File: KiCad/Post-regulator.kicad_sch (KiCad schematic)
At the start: 111 parts, among them IC17 LTC2050HVCS8#PBF, IC18 TL072D, IC19 TL072D, IC20 SN74LVC1G3157DCKR, Q10 MMBT5401, Q11 MMBT5401, Q12 BCP56-16.115, Q13 MMBT5551, Q14 IRFP250NPBF, Q15 BCP56-16.115, Q16 BC857C, Q17 IRFI9Z34GPBF, Q18 PSMN0R9-25YLC, Q19 PSMN0R9-25YLC, Q9 MMBT5551

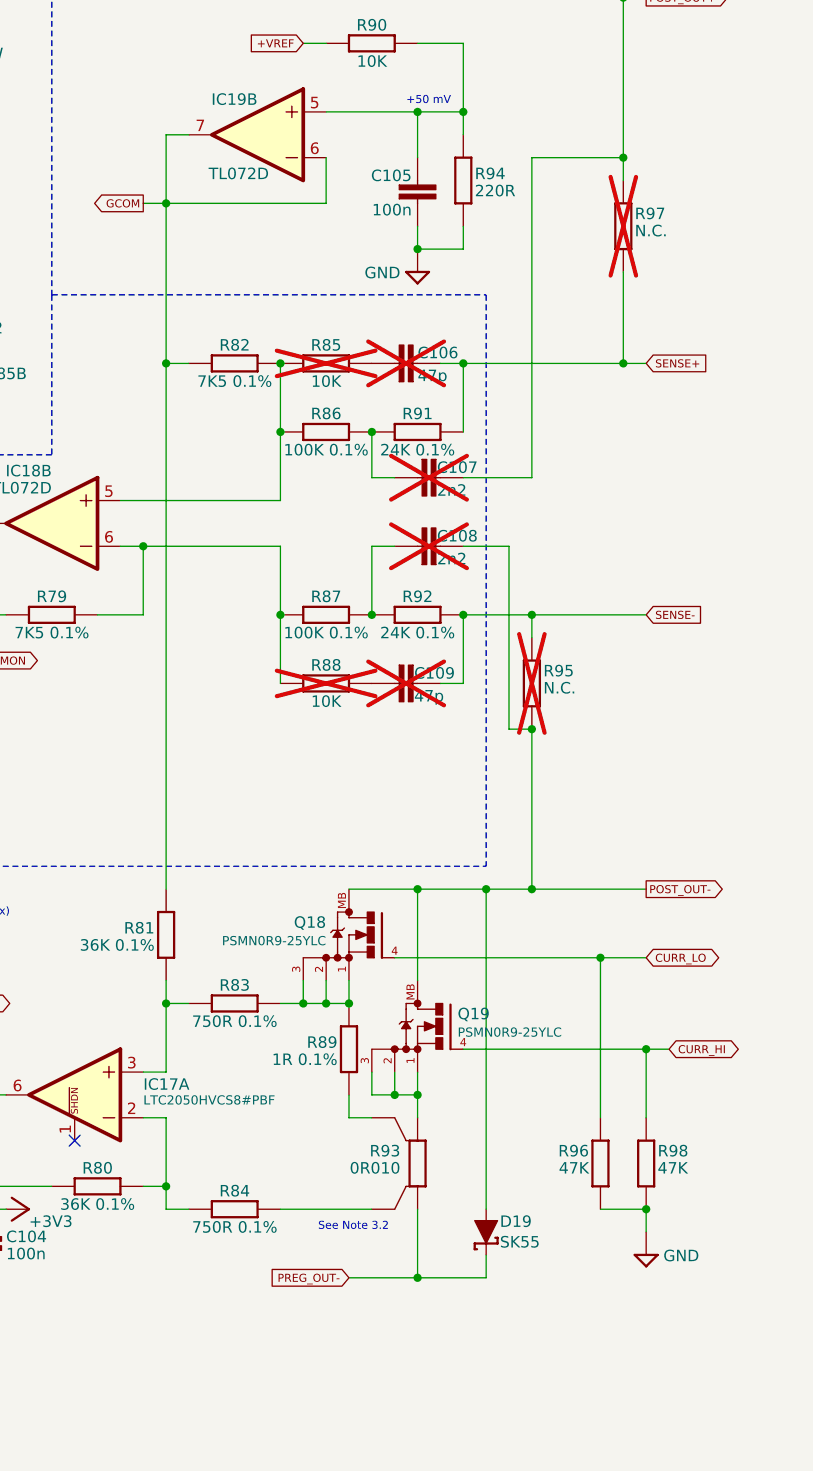
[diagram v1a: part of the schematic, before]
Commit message: DIB connector update
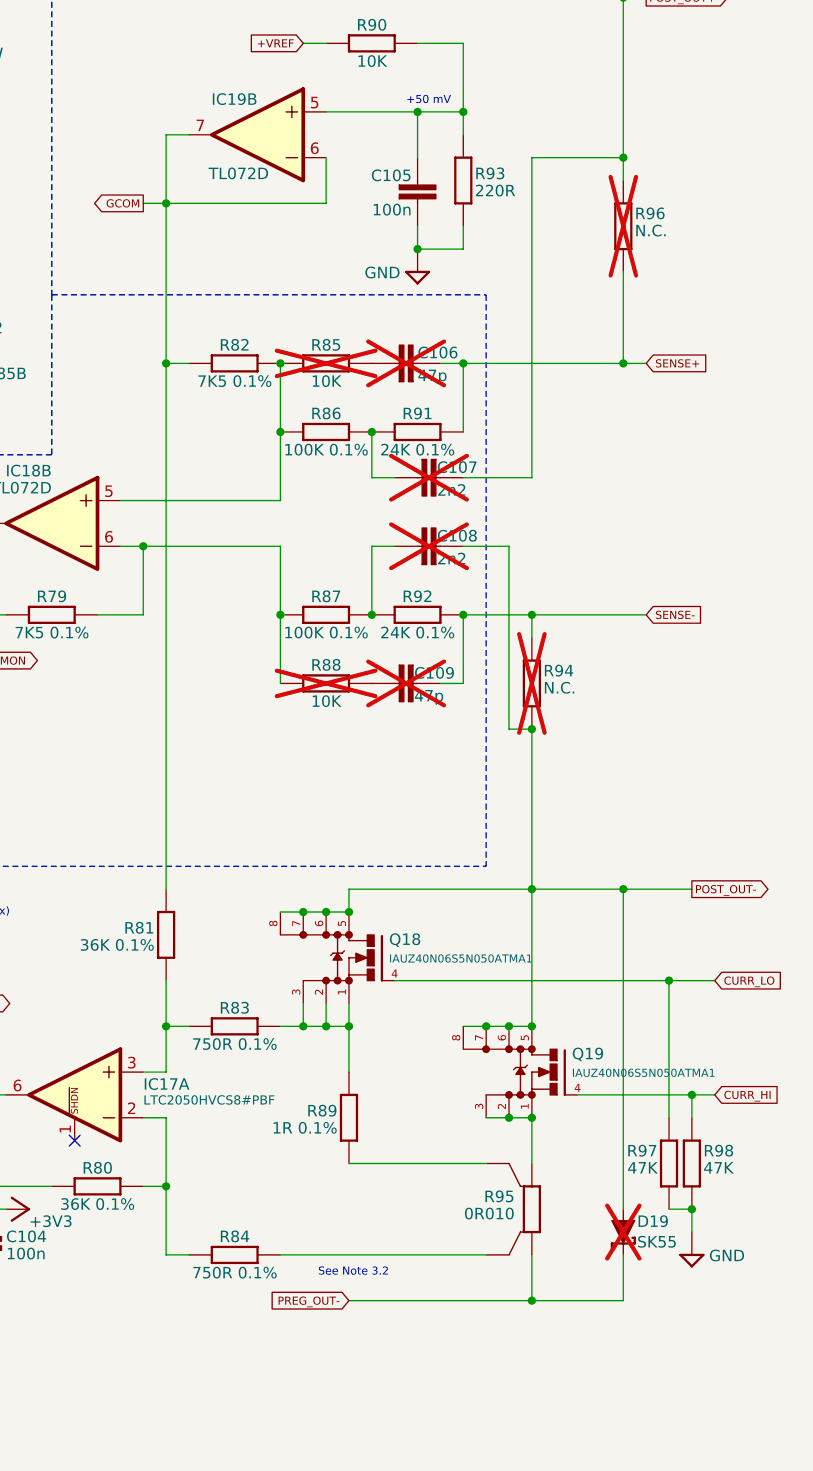
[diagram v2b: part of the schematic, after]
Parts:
- removed Q18, Q19: PSMN0R9-25YLC, PCM_EEZ_SMD:SOT669, symbol PCM_EEZ_discretes:NMOS_LFPAK
- added Q18, Q19: IAUZ40N06S5N050ATMA1, PCM_EEZ_SMD:TDSON-8, symbol PCM_EEZ_discretes:NMOS_TDSON-8
- D19: now not fitted; now left out of the parts list
- renumbered R94 to R93, R95 to R94, R93 to R95, R97 to R96, R96 to R97
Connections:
- net CURR_HI: now also Q19.4 (G)
- net CURR_LO: now also Q18.4 (G)
- net POST_OUT-: now also Q18.5 (D), Q18.6 (S), Q18.7 (S), Q18.8 (S), Q19.5 (D), Q19.6 (S), Q19.7 (S), Q19.8 (S)
- net at R83.1, R89.2: now also Q18.1 (S), Q18.2 (S), Q18.3 (S)
- net at R95.2: now also Q19.1 (S), Q19.2 (S), Q19.3 (S)
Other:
- moved on the sheet: R83, R84, R89, R95, R97, R98

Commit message: Gerbers update
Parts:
- renumbered C101 to C100, C102 to C101, C103 to C102, C104 to C103, C105 to C104, C106 to C105, C107 to C106, C108 to C107, C109 to C108, C85 to C84, C86 to C85, C87 to C86, C88 to C87, C89 to C88, C90 to C89, C91 to C90, C92 to C91, C93 to C92, C94 to C93, C95 to C94, C96 to C95, C97 to C96, C98 to C97, C99 to C98, C100 to C99, ZD3 to ZD4, ZD4 to ZD5
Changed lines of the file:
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@@
 	(title_block
 		(title "${project_name}")
-		(date "2026-01-06")
+		(date "2026-01-13")
 		(rev "${project_version}")
 		(company "${project_creator}")
@@
 		(on_board yes)
 		(dnp no)
-		(property "Reference" "ZD3"
+		(property "Reference" "ZD4"
 			(at 111.252 30.48 90)
 			(effects
@@
 			(project "EEZ DIB DCP405"
 				(path "/65943c0e-8943-4d2a-93dc-fb4938f73312/34bb83a5-d559-4d80-b3e4-82ef079c17b9"
-					(reference "ZD3")
+					(reference "ZD4")
 					(unit 1)
 				)
@@
 		(on_board yes)
 		(dnp no)
-		(property "Reference" "C90"
+		(property "Reference" "C89"
 			(at 45.339 146.939 90)
 			(effects
@@
 			(project "EEZ DIB DCP405"
 				(path "/65943c0e-8943-4d2a-93dc-fb4938f73312/34bb83a5-d559-4d80-b3e4-82ef079c17b9"
-					(reference "C90")
+					(reference "C89")
 					(unit 1)
 				)
@@
 		(on_board yes)
 		(dnp no)
-		(property "Reference" "C93"
+		(property "Reference" "C92"
 			(at 63.119 146.939 90)
 			(effects
@@
 			(project "EEZ DIB DCP405"
 				(path "/65943c0e-8943-4d2a-93dc-fb4938f73312/34bb83a5-d559-4d80-b3e4-82ef079c17b9"
-					(reference "C93")
+					(reference "C92")
 					(unit 1)
 				)
@@
 		(on_board yes)
 		(dnp no)
-		(property "Reference" "ZD4"
+		(property "Reference" "ZD5"
 			(at 142.24 38.735 0)
 			(effects
@@
 			(project "EEZ DIB DCP405"
 				(path "/65943c0e-8943-4d2a-93dc-fb4938f73312/34bb83a5-d559-4d80-b3e4-82ef079c17b9"
-					(reference "ZD4")
+					(reference "ZD5")
 					(unit 1)
 				)
@@
 		(on_board yes)
 		(dnp no)
-		(property "Reference" "C91"
+		(property "Reference" "C90"
 			(at 46.101 51.816 0)
 			(effects
@@
 			(project "EEZ DIB DCP405"
 				(path "/65943c0e-8943-4d2a-93dc-fb4938f73312/34bb83a5-d559-4d80-b3e4-82ef079c17b9"
-					(reference "C91")
+					(reference "C90")
 					(unit 1)
 				)
@@
 		(on_board yes)
 		(dnp no)
-		(property "Reference" "C89"
+		(property "Reference" "C88"
 			(at 45.339 126.619 90)
 			(effects
@@
 			(project "EEZ DIB DCP405"
 				(path "/65943c0e-8943-4d2a-93dc-fb4938f73312/34bb83a5-d559-4d80-b3e4-82ef079c17b9"
-					(reference "C89")
+					(reference "C88")
 					(unit 1)
 				)
@@
 		(on_board yes)
 		(dnp no)
-		(property "Reference" "C102"
+		(property "Reference" "C101"
 			(at 167.894 108.839 90)
 			(effects
@@
 			(project "EEZ DIB DCP405"
 				(path "/65943c0e-8943-4d2a-93dc-fb4938f73312/34bb83a5-d559-4d80-b3e4-82ef079c17b9"
-					(reference "C102")
+					(reference "C101")
 					(unit 1)
 				)
@@
 		(on_board yes)
 		(dnp no)
-		(property "Reference" "C92"
+		(property "Reference" "C91"
 			(at 63.119 126.619 90)
 			(effects
@@
 			(project "EEZ DIB DCP405"
 				(path "/65943c0e-8943-4d2a-93dc-fb4938f73312/34bb83a5-d559-4d80-b3e4-82ef079c17b9"
-					(reference "C92")
+					(reference "C91")
 					(unit 1)
 				)
@@
 		(on_board yes)
 		(dnp yes)
-		(property "Reference" "C108"
+		(property "Reference" "C107"
 			(at 243.459 78.359 90)
 			(effects
@@
 			(project "EEZ DIB DCP405"
 				(path "/65943c0e-8943-4d2a-93dc-fb4938f73312/34bb83a5-d559-4d80-b3e4-82ef079c17b9"
-					(reference "C108")
+					(reference "C107")
 					(unit 1)
 				)
@@
 		(on_board yes)
 		(dnp no)
-		(property "Reference" "C96"
+		(property "Reference" "C95"
 			(at 99.441 66.929 0)
 			(effects
@@
 			(project "EEZ DIB DCP405"
 				(path "/65943c0e-8943-4d2a-93dc-fb4938f73312/34bb83a5-d559-4d80-b3e4-82ef079c17b9"
-					(reference "C96")
+					(reference "C95")
 					(unit 1)
 				)
@@
 		(on_board yes)
 		(dnp no)
-		(property "Reference" "C99"
+		(property "Reference" "C98"
 			(at 140.081 94.361 90)
 			(effects
@@
 			(project "EEZ DIB DCP405"
 				(path "/65943c0e-8943-4d2a-93dc-fb4938f73312/34bb83a5-d559-4d80-b3e4-82ef079c17b9"
-					(reference "C99")
+					(reference "C98")
 					(unit 1)
 				)
@@
 		(on_board yes)
 		(dnp no)
-		(property "Reference" "C97"
+		(property "Reference" "C96"
 			(at 129.286 172.339 90)
 			(effects
@@
 			(project "EEZ DIB DCP405"
 				(path "/65943c0e-8943-4d2a-93dc-fb4938f73312/34bb83a5-d559-4d80-b3e4-82ef079c17b9"
-					(reference "C97")
+					(reference "C96")
 					(unit 1)
 				)
@@
 		(on_board yes)
 		(dnp no)
-		(property "Reference" "C85"
+		(property "Reference" "C84"
 			(at 30.861 124.841 90)
 			(effects
@@
 			(project "EEZ DIB DCP405"
 				(path "/65943c0e-8943-4d2a-93dc-fb4938f73312/34bb83a5-d559-4d80-b3e4-82ef079c17b9"
-					(reference "C85")
+					(reference "C84")
 					(unit 1)
 				)
@@
 		(on_board yes)
 		(dnp no)
-		(property "Reference" "C100"
+		(property "Reference" "C99"
 			(at 164.719 90.424 0)
 			(effects
@@
 			(project "EEZ DIB DCP405"
 				(path "/65943c0e-8943-4d2a-93dc-fb4938f73312/34bb83a5-d559-4d80-b3e4-82ef079c17b9"
-					(reference "C100")
+					(reference "C99")
 					(unit 1)
 				)
@@
 		(on_board yes)
 		(dnp no)
-		(property "Reference" "C98"
+		(property "Reference" "C97"
 			(at 129.921 147.701 90)
 			(effects
@@
 			(project "EEZ DIB DCP405"
 				(path "/65943c0e-8943-4d2a-93dc-fb4938f73312/34bb83a5-d559-4d80-b3e4-82ef079c17b9"
-					(reference "C98")
+					(reference "C97")
 					(unit 1)
 				)
@@
 		(on_board yes)
 		(dnp no)
-		(property "Reference" "C88"
+		(property "Reference" "C87"
 			(at 30.861 145.161 90)
 			(effects
@@
 			(project "EEZ DIB DCP405"
 				(path "/65943c0e-8943-4d2a-93dc-fb4938f73312/34bb83a5-d559-4d80-b3e4-82ef079c17b9"
-					(reference "C88")
+					(reference "C87")
 					(unit 1)
 				)
@@
 		(on_board yes)
 		(dnp no)
-		(property "Reference" "C104"
+		(property "Reference" "C103"
 			(at 195.58 156.21 0)
 			(effects
@@
 			(project "EEZ DIB DCP405"
 				(path "/65943c0e-8943-4d2a-93dc-fb4938f73312/34bb83a5-d559-4d80-b3e4-82ef079c17b9"
-					(reference "C104")
+					(reference "C103")
 					(unit 1)
 				)
@@
 		(on_board yes)
 		(dnp no)
-		(property "Reference" "C101"
+		(property "Reference" "C100"
 			(at 162.941 125.984 0)
 			(effects
@@
 			(project "EEZ DIB DCP405"
 				(path "/65943c0e-8943-4d2a-93dc-fb4938f73312/34bb83a5-d559-4d80-b3e4-82ef079c17b9"
-					(reference "C101")
+					(reference "C100")
 					(unit 1)
 				)
@@
 		(on_board yes)
 		(dnp yes)
-		(property "Reference" "C107"
+		(property "Reference" "C106"
 			(at 243.459 70.739 90)
 			(effects
@@
 			(project "EEZ DIB DCP405"
 				(path "/65943c0e-8943-4d2a-93dc-fb4938f73312/34bb83a5-d559-4d80-b3e4-82ef079c17b9"
-					(reference "C107")
+					(reference "C106")
 					(unit 1)
 				)
@@
 		(on_board yes)
 		(dnp no)
-		(property "Reference" "C95"
+		(property "Reference" "C94"
 			(at 88.519 146.939 90)
 			(effects
@@
 			(project "EEZ DIB DCP405"
 				(path "/65943c0e-8943-4d2a-93dc-fb4938f73312/34bb83a5-d559-4d80-b3e4-82ef079c17b9"
-					(reference "C95")
+					(reference "C94")
 					(unit 1)
 				)
@@
 		(on_board yes)
 		(dnp no)
-		(property "Reference" "C103"
+		(property "Reference" "C102"
 			(at 172.974 73.279 90)
 			(effects
@@
 			(project "EEZ DIB DCP405"
 				(path "/65943c0e-8943-4d2a-93dc-fb4938f73312/34bb83a5-d559-4d80-b3e4-82ef079c17b9"
-					(reference "C103")
+					(reference "C102")
 					(unit 1)
 				)
@@
 		(on_board yes)
 		(dnp no)
-		(property "Reference" "C105"
+		(property "Reference" "C104"
 			(at 240.665 36.83 0)
 			(effects
@@
 			(project "EEZ DIB DCP405"
 				(path "/65943c0e-8943-4d2a-93dc-fb4938f73312/34bb83a5-d559-4d80-b3e4-82ef079c17b9"
-					(reference "C105")
+					(reference "C104")
 					(unit 1)
 				)
@@
 		(on_board yes)
 		(dnp no)
-		(property "Reference" "C87"
+		(property "Reference" "C86"
 			(at 30.861 140.081 90)
 			(effects
@@
 			(project "EEZ DIB DCP405"
 				(path "/65943c0e-8943-4d2a-93dc-fb4938f73312/34bb83a5-d559-4d80-b3e4-82ef079c17b9"
-					(reference "C87")
+					(reference "C86")
 					(unit 1)
 				)
@@
 		(on_board yes)
 		(dnp no)
-		(property "Reference" "C94"
+		(property "Reference" "C93"
 			(at 88.519 126.619 90)
 			(effects
@@
 			(project "EEZ DIB DCP405"
 				(path "/65943c0e-8943-4d2a-93dc-fb4938f73312/34bb83a5-d559-4d80-b3e4-82ef079c17b9"
-					(reference "C94")
+					(reference "C93")
 					(unit 1)
 				)
@@
 		(on_board yes)
 		(dnp yes)
-		(property "Reference" "C109"
+		(property "Reference" "C108"
 			(at 240.919 93.599 90)
 			(effects
@@
 			(project "EEZ DIB DCP405"
 				(path "/65943c0e-8943-4d2a-93dc-fb4938f73312/34bb83a5-d559-4d80-b3e4-82ef079c17b9"
-					(reference "C109")
+					(reference "C108")
 					(unit 1)
 				)
@@
 		(on_board yes)
 		(dnp yes)
-		(property "Reference" "C106"
+		(property "Reference" "C105"
 			(at 241.3 56.515 90)
 			(effects
@@
 			(project "EEZ DIB DCP405"
 				(path "/65943c0e-8943-4d2a-93dc-fb4938f73312/34bb83a5-d559-4d80-b3e4-82ef079c17b9"
-					(reference "C106")
+					(reference "C105")
 					(unit 1)
 				)
@@
 		(on_board yes)
 		(dnp no)
-		(property "Reference" "C86"
+		(property "Reference" "C85"
 			(at 30.861 129.921 90)
 			(effects
@@
 			(project "EEZ DIB DCP405"
 				(path "/65943c0e-8943-4d2a-93dc-fb4938f73312/34bb83a5-d559-4d80-b3e4-82ef079c17b9"
-					(reference "C86")
+					(reference "C85")
 					(unit 1)
 				)

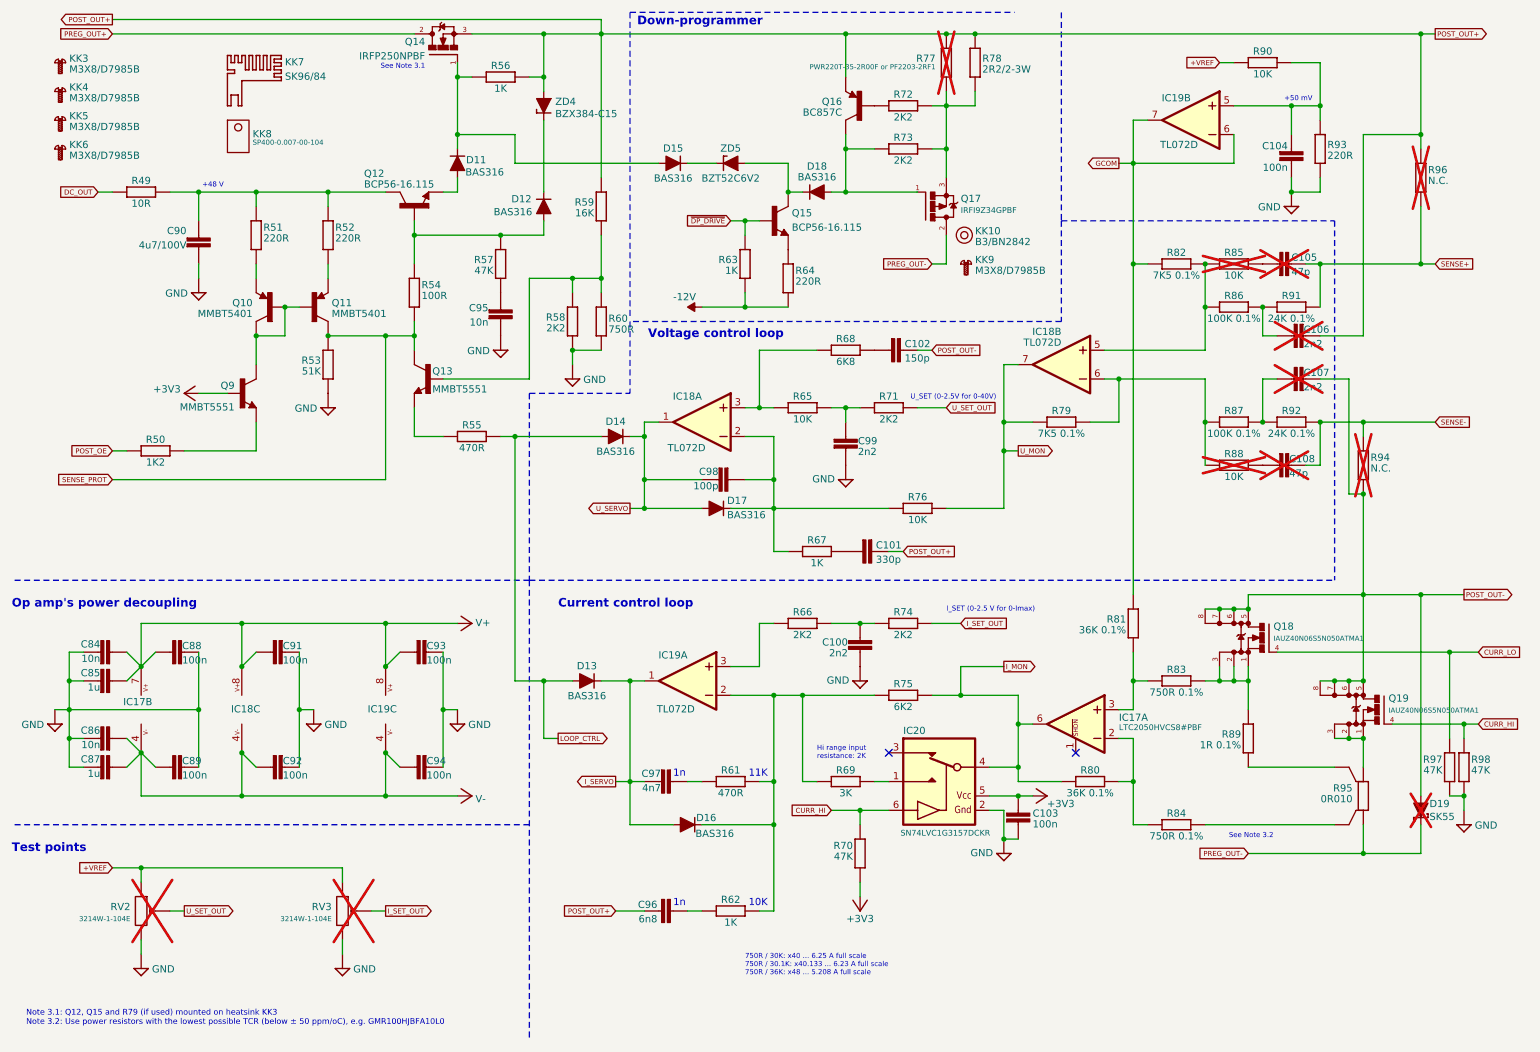
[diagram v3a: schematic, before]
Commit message: Q18, Q19 model fixed
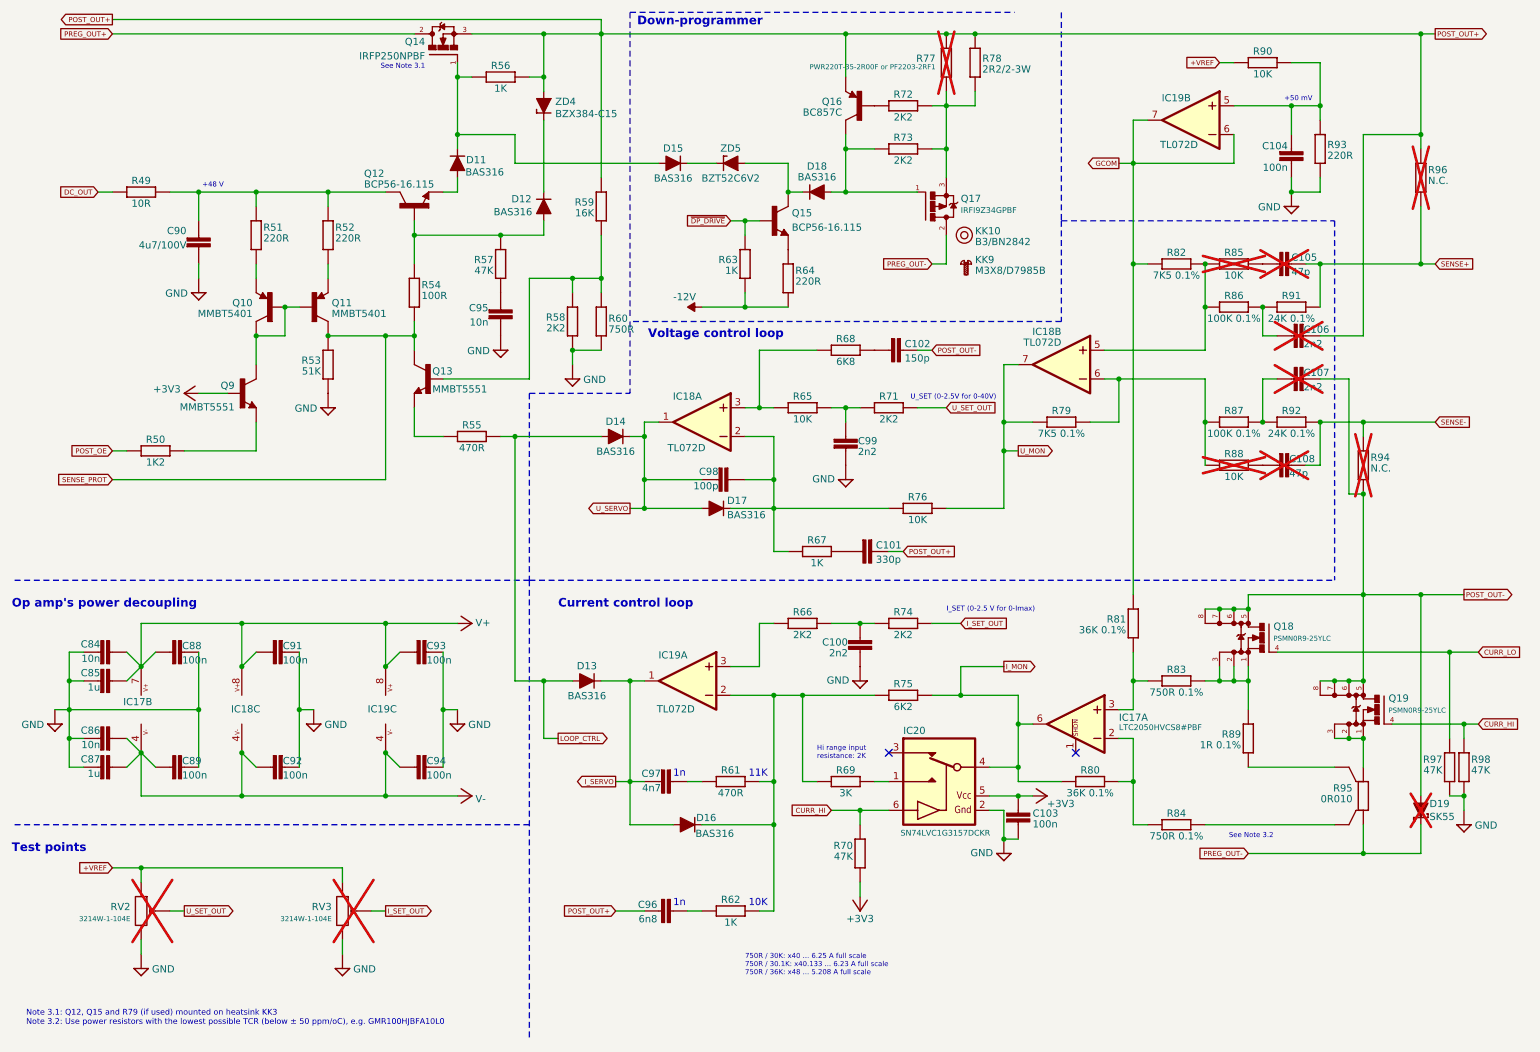
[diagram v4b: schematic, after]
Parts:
- removed KK3, KK4, KK5, KK6: M3X8/D7985B, symbol PCM_EEZ_unsorted:M3X8/D7985B
- removed KK7: SK96/84, PCM_EEZ_unsorted:SK96_84, symbol PCM_EEZ_unsorted:SK96/84SA
- removed KK8: SP400-0.007-00-104, symbol PCM_EEZ_unsorted:TO247_Thermal_pad
- Q18, Q19: value IAUZ40N06S5N050ATMA1 -> PSMN0R9-25YLC; DigiKey 448-IAUZ40N06S5N050ATMA1CT-ND -> 1727-5292-1-ND; LCSC C3289320 -> C179450; Mouser 726-IAUZ40N06S5N050A -> 771-PSMN0R925YLC115; TME - -> PSMN0R9-25YLC.115

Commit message: #2, #3, image of the assembled module
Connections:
- net POST_OE renamed ~{POST_OE}
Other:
- moved on the sheet: IC19A
